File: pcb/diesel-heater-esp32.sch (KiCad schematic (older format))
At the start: 27 parts, among them J1 5V Power, J10 Fan Motor, J11 Glow Plug, J12 Oil Pump, J2 ESP32 Left, J3 Hall Sensor, J4 Buttons, J5 Battery Mon, J6 ESP32 Right, J7 OLED, J8 NTC50K Room Temperatire, J9 NTC50K Outlet Temperatire

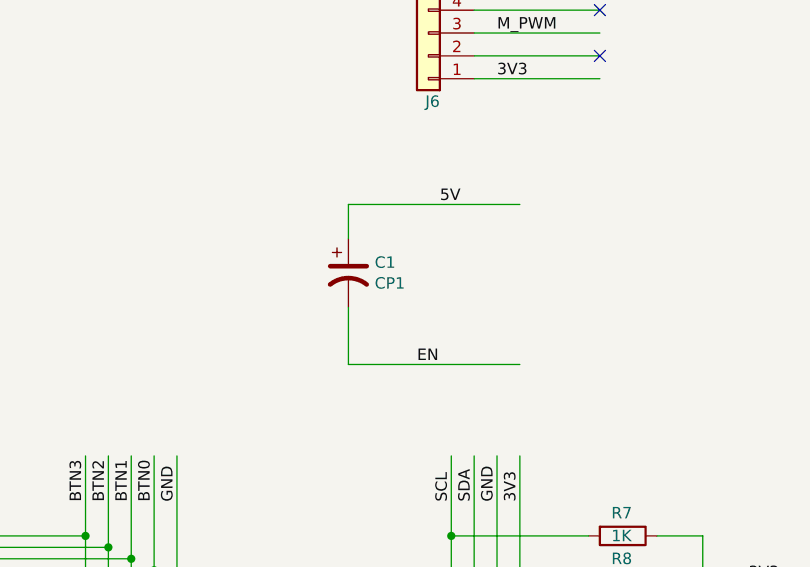
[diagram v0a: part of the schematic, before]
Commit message: capacitor value fixed. capacitor sized set to 6.3mm
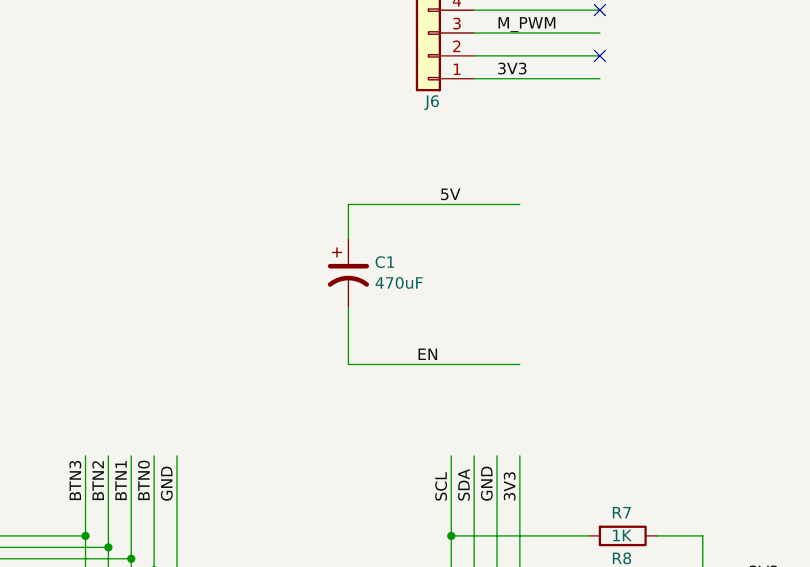
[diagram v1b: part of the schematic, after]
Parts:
- C1: value CP1 -> 470uF; footprint Capacitor_THT:CP_Radial_D7.5mm_P2.50mm -> Capacitor_THT:CP_Radial_D6.3mm_P2.50mm
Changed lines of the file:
@@
 P 4050 5300
 F 0 "C1" H 4165 5346 50  0000 L CNN
-F 1 "CP1" H 4165 5255 50  0000 L CNN
-F 2 "Capacitor_THT:CP_Radial_D7.5mm_P2.50mm" H 4050 5300 50  0001 C CNN
+F 1 "470uF" H 4165 5255 50  0000 L CNN
+F 2 "Capacitor_THT:CP_Radial_D6.3mm_P2.50mm" H 4050 5300 50  0001 C CNN
 F 3 "~" H 4050 5300 50  0001 C CNN
 	1    4050 5300

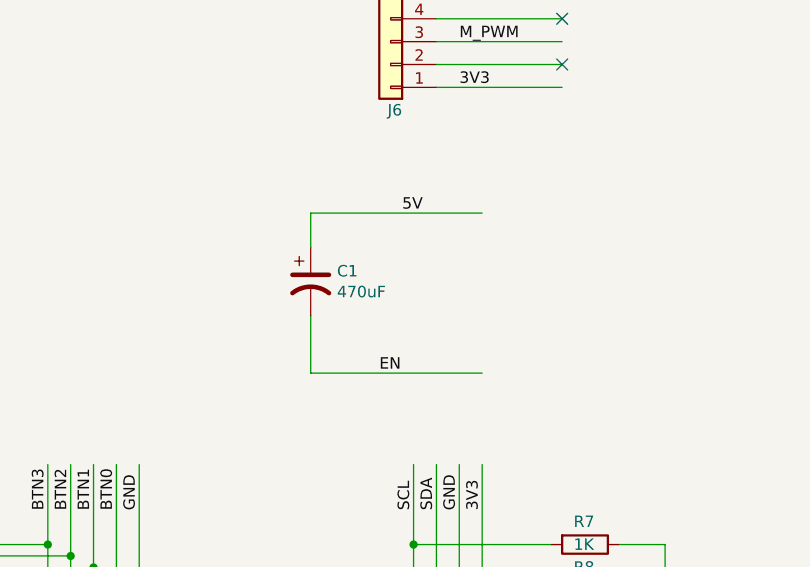
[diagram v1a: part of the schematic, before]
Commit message: fixed bug in en bug workaround circult. capacitor should be connected to EN and grounded
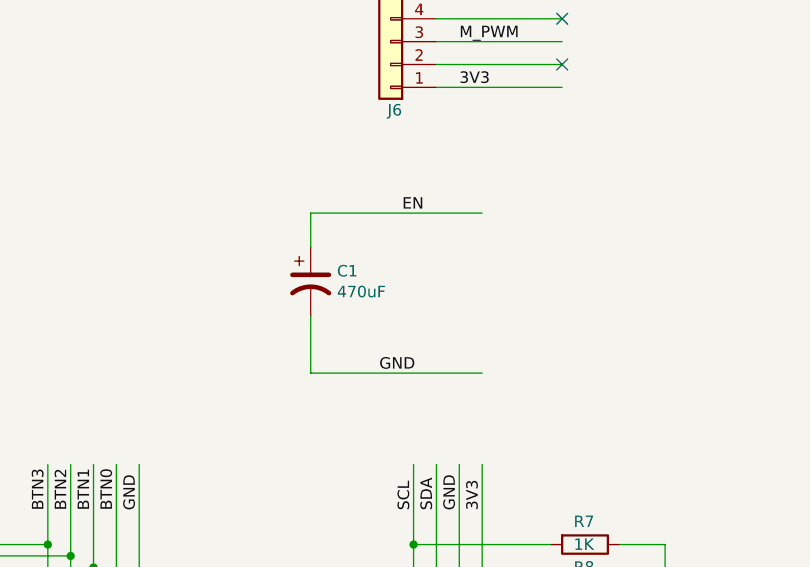
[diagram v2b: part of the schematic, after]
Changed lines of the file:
@@
 	4050 5000 4800 5000
 Text Label 4450 5000 0    50   ~ 0
-5V
+EN
 Wire Wire Line
 	4050 5450 4050 5700
@@
 	4050 5700 4800 5700
 Text Label 4350 5700 0    50   ~ 0
-EN
+GND
 $EndSCHEMATC
